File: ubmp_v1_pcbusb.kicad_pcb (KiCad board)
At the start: 2 copper layers, 38.9 x 14 mm, 26 parts, among them J1 Conn_02x05_Counter_Clockwise, J2 USB_A, U1 NUF8401MNT4G, U2 MIC5245-3.3, U3 STM32F103CBUx, U4 NUF2042XV6T1G, Y1 PRQC8.00CR1010V00L

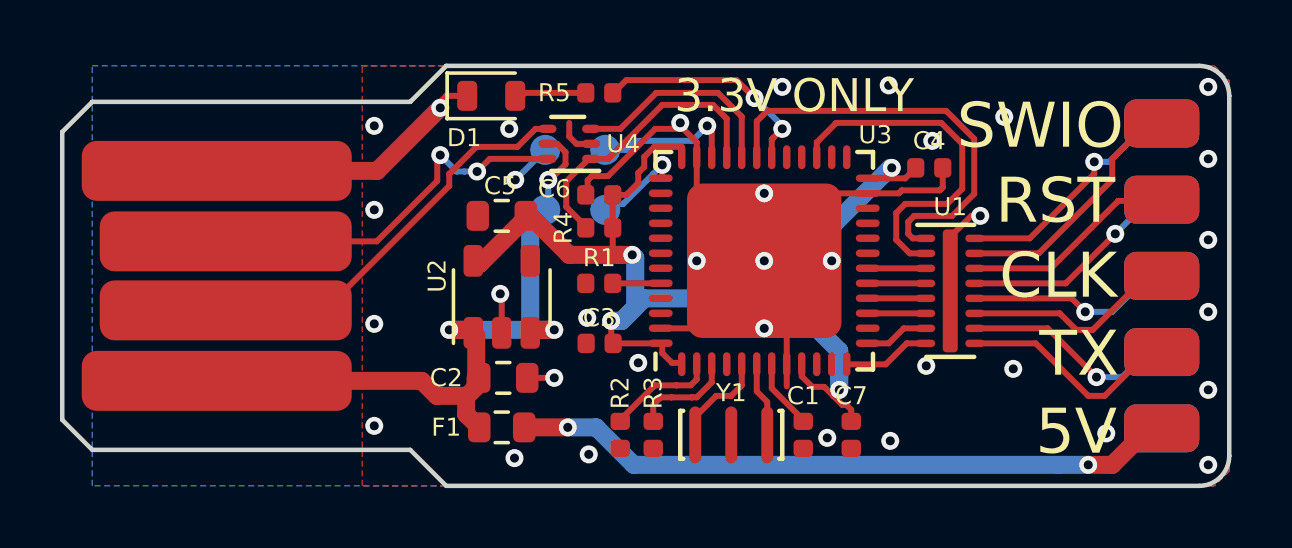
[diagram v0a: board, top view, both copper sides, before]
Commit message: Updated USBPCB version and panel
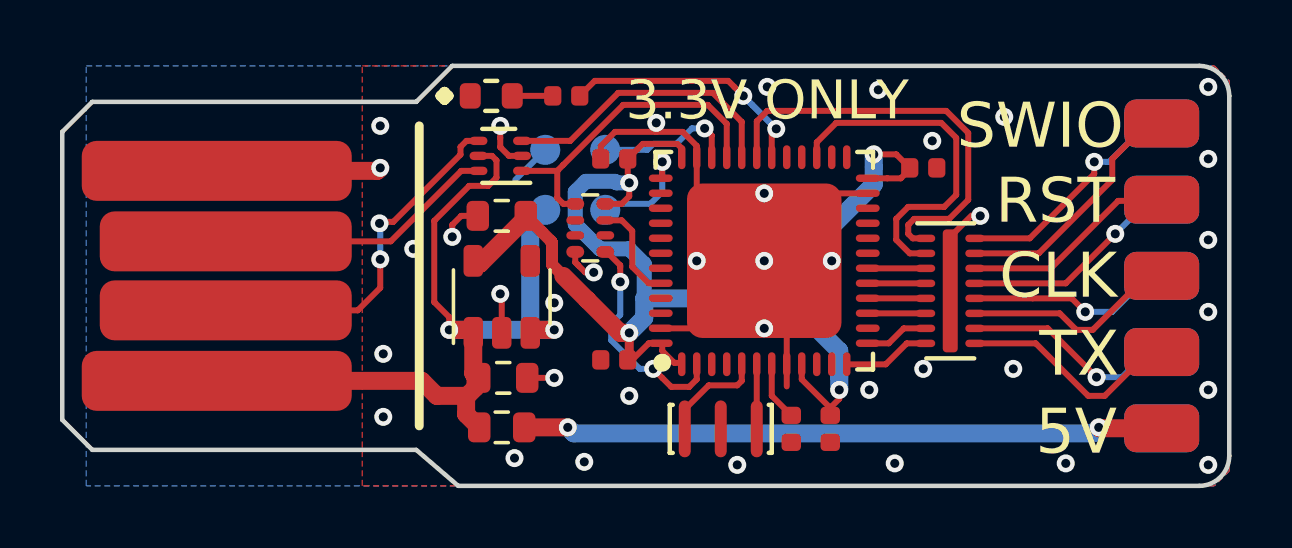
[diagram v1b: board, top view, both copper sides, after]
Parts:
- removed the R1 at (97.5, 106.2)
- removed R2, R3, R4: 1.5k, passive:R_0402_1005Metric_Rounded
- removed REF**: OSHW-Logo2_9.8x8mm_SilkScreen, Symbol:OSHW-Logo2_9.8x8mm_SilkScreen
- added RN1: 1.5k, passive:R_Array_Convex_4x0402, F.Cu at (97.2, 104.4)
- D1: footprint passive:D_0603_1608Metric_Rounded -> leds:LEDC1608X60
- moved U4 2.33 mm to (94.2, 102.0)
- moved C6 1.30 mm to (98.0, 102.1)
- moved R1 1.10 mm to (96.4, 100.0)
- moved C3 0.73 mm to (98.0, 108.8)
- moved C7 0.73 mm to (105.2, 111.1)
- moved C1 0.45 mm to (103.9, 111.1)
- moved Y1 0.40 mm to (101.5, 111.1)
- moved C4 0.20 mm to (108.3, 102.4)
- renumbered R5 to R1
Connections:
- U3 pad 3: /bmp_core/STM_ID2 -> Net-(U3-Pad3)
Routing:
- net GND: track 44.1 -> 38.4 mm, vias 35 -> 37
- net +5V: track 24.6 -> 29.4 mm, vias 3 -> 2
- net +3V3: track 40.2 -> 44.4 mm
- net /bmp_core/STM_ID: track 3.61 -> 7.43 mm, vias 0 -> 2
- net /bmp_core/STM_ID2: track 3.40 -> 0.00 mm
- net /DP: track 12.8 -> 9.40 mm, vias 2 -> 0
- net /bmp_core/DM_P: track 7.26 -> 9.57 mm
- net /bmp_core/LED_STLINK: track 7.82 -> 9.94 mm
- net /bmp_core/BOOT0: track 1.70 -> 3.42 mm
- net /DM: track 13.5 -> 12.2 mm, vias 0 -> 2
- net /bmp_core/DP_P: track 9.67 -> 10.7 mm
- net Net-(D1-Pad2): track 2.15 -> 1.25 mm
- net Net-(F1-Pad1): track 22.3 -> 21.4 mm
- net /bmp_core/SWCLK: track 2.89 -> 3.62 mm
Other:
- outline, holes or cut-outs redrawn
